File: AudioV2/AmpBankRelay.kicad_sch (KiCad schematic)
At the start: 20 parts, among them K301 AZ850P2-5, K302 AZ850P2-5, K303 AZ850P2-5, K304 AZ850P2-5, U321 TBD62083APG

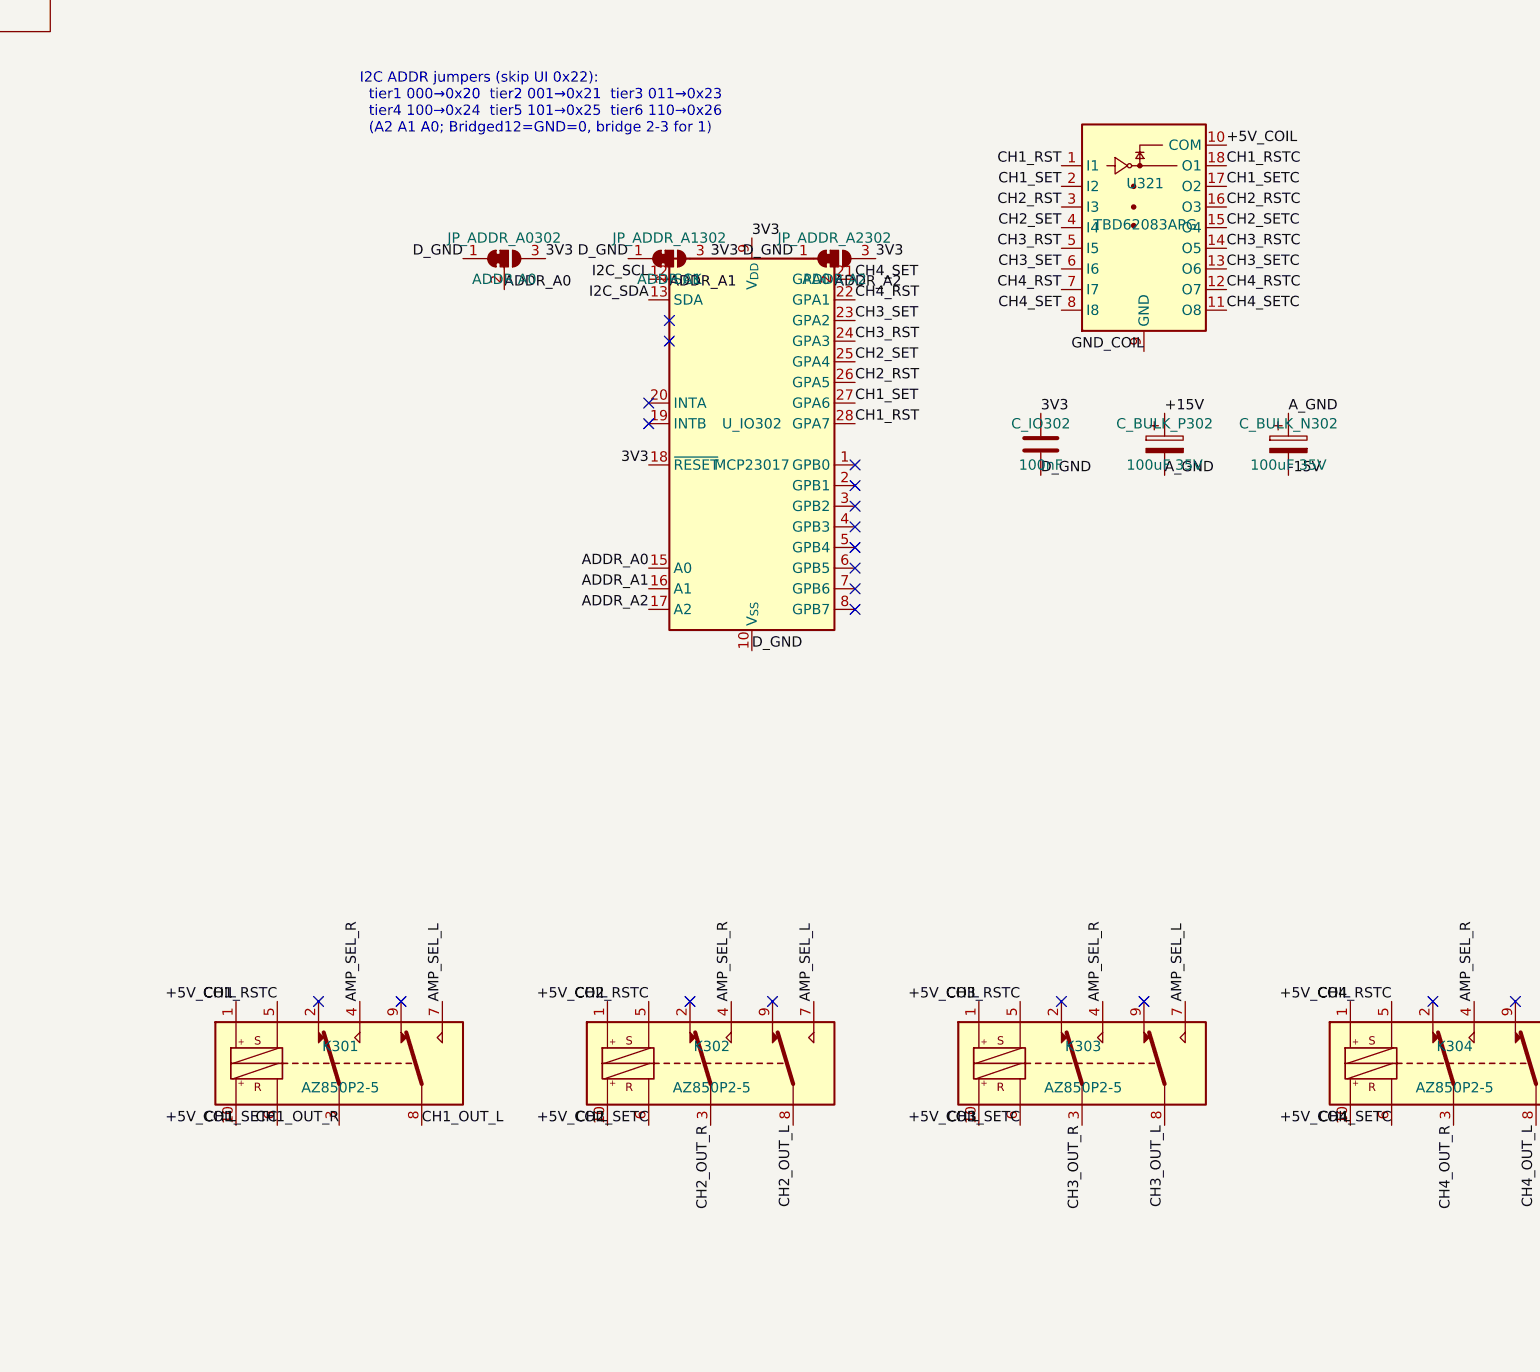
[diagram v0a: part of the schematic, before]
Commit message: AudioV2: AZ850 の SETC/RSTC を DS どおりに揃え、Relay PCB を追従
コイル pin5=SETC / pin6=RSTC に直し、接点は reset 側 4/7=バスのまま。生成スクリプトも sch/PCB に合わせた。

Co-authored-by: Cursor <cursoragent@cursor.com>
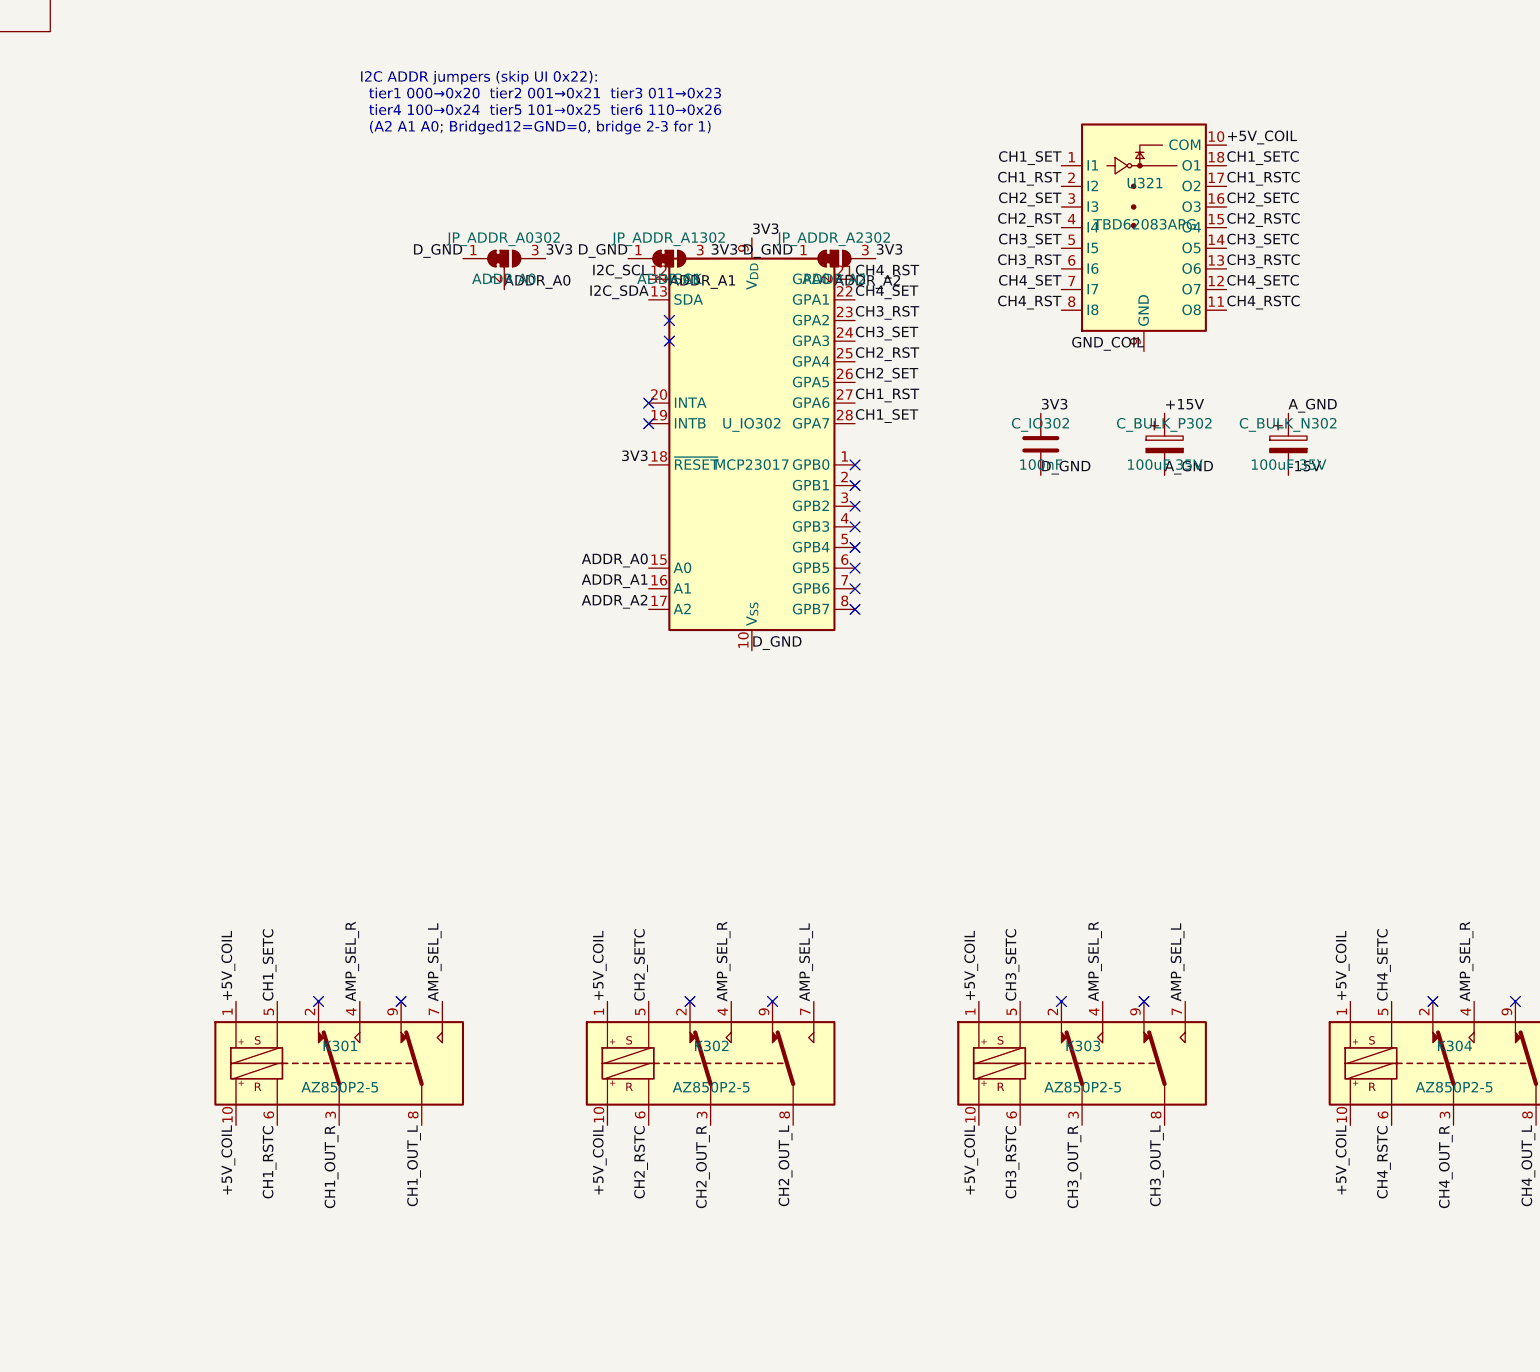
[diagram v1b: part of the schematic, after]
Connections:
- net CH1_RST: now also U321.2 (I2), U_IO302.27 (GPA6); no longer U321.1 (I1), U_IO302.28 (GPA7)
- net CH1_RSTC: now also K301.6, U321.17 (O2); no longer K301.5, U321.18 (O1)
- net CH1_SET: now also U321.1 (I1), U_IO302.28 (GPA7); no longer U321.2 (I2), U_IO302.27 (GPA6)
- net CH1_SETC: now also K301.5, U321.18 (O1); no longer K301.6, U321.17 (O2)
- net CH2_RST: now also U321.4 (I4), U_IO302.25 (GPA4); no longer U321.3 (I3), U_IO302.26 (GPA5)
- net CH2_RSTC: now also K302.6, U321.15 (O4); no longer K302.5, U321.16 (O3)
- net CH2_SET: now also U321.3 (I3), U_IO302.26 (GPA5); no longer U321.4 (I4), U_IO302.25 (GPA4)
- net CH2_SETC: now also K302.5, U321.16 (O3); no longer K302.6, U321.15 (O4)
- net CH3_RST: now also U321.6 (I6), U_IO302.23 (GPA2); no longer U321.5 (I5), U_IO302.24 (GPA3)
- net CH3_RSTC: now also K303.6, U321.13 (O6); no longer K303.5, U321.14 (O5)
- net CH3_SET: now also U321.5 (I5), U_IO302.24 (GPA3); no longer U321.6 (I6), U_IO302.23 (GPA2)
- net CH3_SETC: now also K303.5, U321.14 (O5); no longer K303.6, U321.13 (O6)
- net CH4_RST: now also U321.8 (I8), U_IO302.21 (GPA0); no longer U321.7 (I7), U_IO302.22 (GPA1)
- net CH4_RSTC: now also K304.6, U321.11 (O8); no longer K304.5, U321.12 (O7)
- net CH4_SET: now also U321.7 (I7), U_IO302.22 (GPA1); no longer U321.8 (I8), U_IO302.21 (GPA0)
- net CH4_SETC: now also K304.5, U321.12 (O7); no longer K304.6, U321.11 (O8)
